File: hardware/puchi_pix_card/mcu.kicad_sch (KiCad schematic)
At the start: 47 parts, among them J1 USB_C_Receptacle_USB2.0_14P, J2 Conn_01x04, J3 Conn_01x10, J4 Conn_01x10, SW1 VBAT_SW, SW2 SW_Push, SW3 SW_Push, U1 TPS61023DRL, U2 XC6206PxxxMR, U3 STM32G0B1CBTx, U4 XC6206PxxxMR, U5 USBLC6-2SC6, U6 KXTJ3-1057, U7 W25Q64JVSSIQ

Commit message: Fix design-review findings: I2C/PFET-gate pull-ups, red-column VDROP, D1/L1 part selection, USB-C 16P, USB power policy, MBI GCLK dead time and sleep leak paths
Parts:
- added C16: 22pF, symbol Device:C
- added R13, R14: 2.2k, symbol Device:R
- D1: value D_Schottky -> B5819W; footprint (none) -> Diode_SMD:D_SOD-123
- D2, D3: value D_Schottky -> BAT54; footprint (none) -> Diode_SMD:D_SOD-323
- J1: value USB_C_Receptacle_USB2.0_14P -> USB_C_Receptacle_USB2.0_16P; symbol Connector:USB_C_Receptacle_USB2.0_14P -> Connector:USB_C_Receptacle_USB2.0_16P
- L1: value 1uH -> SWPA4030S1R0MT; LCSC (none) -> C316359
- R10, R11: value 4.7M -> 1M
- R6, R7: value 100k -> 10k
- R8: value 10k -> 2.2k
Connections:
- net +5V: now also C16.2
- net PB6: now also R13.2
- net PB7: now also R14.2
- net at C14.1, C5.1, C6.1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: now also R13.1, R14.1
- net at R1.2, R2.2, U1.1 (FB): now also C16.1
- no-connect marks 5 -> 7

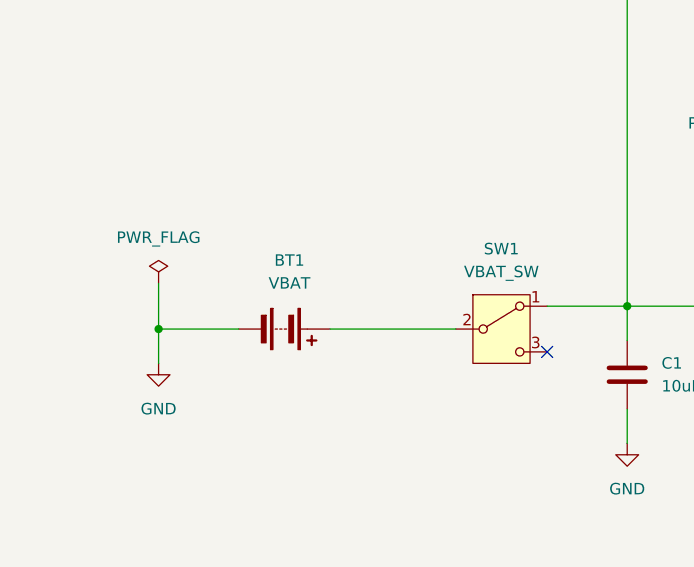
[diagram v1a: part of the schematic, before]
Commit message: Assign footprints: project footprint library (LED/MBI/inductor/switches) and bulk 0402/0805 pass
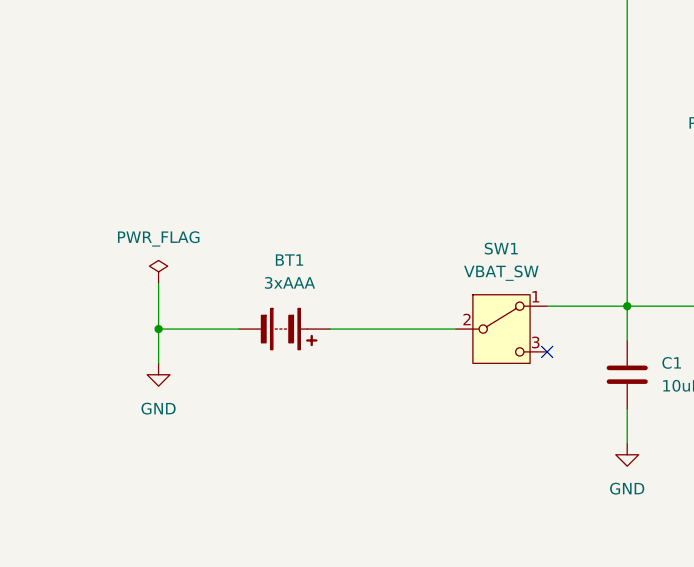
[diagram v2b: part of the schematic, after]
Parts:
- BT1: value VBAT -> 3xAAA
- C1, C2, C3: footprint (none) -> Capacitor_SMD:C_0805_2012Metric
- C10, C11, C12, C13, C14, C15, C16, C4, C5, C6, C7, C8, C9: footprint (none) -> Capacitor_SMD:C_0402_1005Metric
- D4: footprint (none) -> LED_SMD:LED_0603_1608Metric
- J1: footprint (none) -> Connector_USB:USB_C_Receptacle_HRO_TYPE-C-31-M-12
- J2: footprint (none) -> Connector_PinHeader_2.54mm:PinHeader_1x04_P2.54mm_Vertical
- J3, J4: footprint (none) -> Connector_PinHeader_2.54mm:PinHeader_1x10_P2.54mm_Vertical
- L1: footprint (none) -> puchi_pix_card:L_SWPA4030S
- R1, R10, R11, R12, R13, R14, R2, R3, R4, R5, R6, R7, R8, R9: footprint (none) -> Resistor_SMD:R_0402_1005Metric
- SW1: footprint (none) -> puchi_pix_card:SW-SMD_MST-12D18G4-SPDT-SLIDE-SWITCH
- SW2, SW3: footprint (none) -> puchi_pix_card:KEY-SMD_4P-L4.2-W3.2-P2.20-LS4.6
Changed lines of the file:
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@@
 			)
 		)
-		(property "Footprint" ""
+		(property "Footprint" "Connector_PinHeader_2.54mm:PinHeader_1x10_P2.54mm_Vertical"
 			(at 398.78 149.86 0)
 			(effects
@@
 			)
 		)
-		(property "Footprint" ""
+		(property "Footprint" "Resistor_SMD:R_0402_1005Metric"
 			(at 212.852 119.38 90)
 			(effects
@@
 			)
 		)
-		(property "Footprint" ""
+		(property "Footprint" "Capacitor_SMD:C_0402_1005Metric"
 			(at 329.8952 50.8 0)
 			(effects
@@
 			)
 		)
-		(property "Footprint" ""
+		(property "Footprint" "Capacitor_SMD:C_0402_1005Metric"
 			(at 174.9552 200.66 0)
 			(effects
@@
 			)
 		)
-		(property "Footprint" ""
+		(property "Footprint" "Resistor_SMD:R_0402_1005Metric"
 			(at 253.492 203.2 90)
 			(effects
@@
 			)
 		)
-		(property "Footprint" ""
+		(property "Footprint" "Capacitor_SMD:C_0805_2012Metric"
 			(at 83.5152 107.95 0)
 			(effects
@@
 			)
 		)
-		(property "Footprint" ""
+		(property "Footprint" "Resistor_SMD:R_0402_1005Metric"
 			(at 102.362 111.76 90)
 			(effects
@@
 			)
 		)
-		(property "Footprint" ""
+		(property "Footprint" "Capacitor_SMD:C_0402_1005Metric"
 			(at 215.5952 200.66 0)
 			(effects
@@
 			)
 		)
-		(property "Footprint" ""
+		(property "Footprint" "Resistor_SMD:R_0402_1005Metric"
 			(at 135.128 111.76 90)
 			(effects
@@
 			)
 		)
-		(property "Footprint" ""
+		(property "Footprint" "Capacitor_SMD:C_0805_2012Metric"
 			(at 164.7952 115.57 0)
 			(effects
@@
 			)
 		)
-		(property "Footprint" ""
+		(property "Footprint" "Capacitor_SMD:C_0402_1005Metric"
 			(at 199.0852 116.84 0)
 			(effects
@@
 			)
 		)
-		(property "Footprint" ""
+		(property "Footprint" "Connector_PinHeader_2.54mm:PinHeader_1x10_P2.54mm_Vertical"
 			(at 398.78 106.68 0)
 			(effects
@@
 			)
 		)
-		(property "Footprint" ""
+		(property "Footprint" "Capacitor_SMD:C_0402_1005Metric"
 			(at 277.8252 201.93 0)
 			(effects
@@
 			)
 		)
-		(property "Value" "VBAT"
+		(property "Value" "3xAAA"
 			(at 45.0215 93.98 90)
 			(effects
@@
 			)
 		)
-		(property "Footprint" ""
+		(property "Footprint" "Resistor_SMD:R_0402_1005Metric"
 			(at 257.81 112.522 90)
 			(effects
@@
 			)
 		)
-		(property "Footprint" ""
+		(property "Footprint" "Capacitor_SMD:C_0402_1005Metric"
 			(at 136.8552 52.07 0)
 			(effects
@@
 			)
 		)
-		(property "Footprint" ""
+		(property "Footprint" "puchi_pix_card:KEY-SMD_4P-L4.2-W3.2-P2.20-LS4.6"
 			(at 232.41 86.36 0)
 			(effects
@@
 			)
 		)
-		(property "Footprint" ""
+		(property "Footprint" "Capacitor_SMD:C_0402_1005Metric"
 			(at 146.05 124.7648 0)
 			(effects
@@
 			)
 		)
-		(property "Footprint" ""
+		(property "Footprint" "puchi_pix_card:KEY-SMD_4P-L4.2-W3.2-P2.20-LS4.6"
 			(at 201.93 49.53 0)
 			(effects
@@
 			)
 		)
-		(property "Footprint" ""
+		(property "Footprint" "LED_SMD:LED_0603_1608Metric"
 			(at 246.38 114.3 0)
 			(effects
@@
 			)
 		)
-		(property "Footprint" ""
+		(property "Footprint" "Capacitor_SMD:C_0402_1005Metric"
 			(at 357.8352 50.8 0)
 			(effects
@@
 			)
 		)
-		(property "Footprint" ""
+		(property "Footprint" "Capacitor_SMD:C_0402_1005Metric"
 			(at 88.5952 142.24 0)
 			(effects
@@
 			)
 		)
-		(property "Footprint" ""
+		(property "Footprint" "Capacitor_SMD:C_0402_1005Metric"
 			(at 343.8652 50.8 0)
 			(effects
@@
 			)
 		)
-		(property "Footprint" ""
+		(property "Footprint" "Capacitor_SMD:C_0402_1005Metric"
 			(at 106.3752 52.07 0)
 			(effects
@@
 			)
 		)
-		(property "Footprint" ""
+		(property "Footprint" "Resistor_SMD:R_0402_1005Metric"
 			(at 69.85 172.212 90)
 			(effects
@@
 			)
 		)
-		(property "Footprint" ""
+		(property "Footprint" "Resistor_SMD:R_0402_1005Metric"
 			(at 77.47 183.642 90)
 			(effects
@@
 			)
 		)
-		(property "Footprint" ""
+		(property "Footprint" "Capacitor_SMD:C_0402_1005Metric"
 			(at 58.1152 162.56 0)
 			(effects
@@
 			)
 		)
-		(property "Footprint" ""
+		(property "Footprint" "Connector_USB:USB_C_Receptacle_HRO_TYPE-C-31-M-12"
 			(at 35.56 193.04 0)
 			(effects
@@
 			)
 		)
-		(property "Footprint" ""
+		(property "Footprint" "Connector_PinHeader_2.54mm:PinHeader_1x04_P2.54mm_Vertical"
 			(at 267.97 59.69 0)
 			(effects
@@
 			)
 		)
-		(property "Footprint" ""
+		(property "Footprint" "Resistor_SMD:R_0402_1005Metric"
 			(at 221.742 119.38 90)
 			(effects
@@
 			)
 		)
-		(property "Footprint" ""
+		(property "Footprint" "Resistor_SMD:R_0402_1005Metric"
 			(at 22.352 264.16 90)
 			(effects
@@
 			)
 		)
-		(property "Footprint" ""
+		(property "Footprint" "puchi_pix_card:L_SWPA4030S"
 			(at 101.6 85.09 0)
 			(effects
@@
 			)
 		)
-		(property "Footprint" ""
+		(property "Footprint" "Capacitor_SMD:C_0402_1005Metric"
 			(at 252.4252 88.9 0)
 			(effects
@@
 			)
 		)
-		(property "Footprint" ""
+		(property "Footprint" "Resistor_SMD:R_0402_1005Metric"
 			(at 218.44 55.372 90)
 			(effects
@@
 			)
 		)
-		(property "Footprint" ""
+		(property "Footprint" "puchi_pix_card:SW-SMD_MST-12D18G4-SPDT-SLIDE-SWITCH"
 			(at 68.58 99.06 0)
 			(effects
@@
 			)
 		)
-		(property "Footprint" ""
+		(property "Footprint" "Resistor_SMD:R_0402_1005Metric"
 			(at 22.352 250.19 90)
 			(effects
@@
 			)
 		)
-		(property "Footprint" ""
+		(property "Footprint" "Resistor_SMD:R_0402_1005Metric"
 			(at 92.202 120.65 90)
 			(effects
@@
 			)
 		)
-		(property "Footprint" ""
+		(property "Footprint" "Capacitor_SMD:C_0805_2012Metric"
 			(at 153.3652 115.57 0)
 			(effects
@@
 			)
 		)
-		(property "Footprint" ""
+		(property "Footprint" "Resistor_SMD:R_0402_1005Metric"
 			(at 92.202 134.62 90)
 			(effects
@@
 			)
 		)
-		(property "Footprint" ""
+		(property "Footprint" "Resistor_SMD:R_0402_1005Metric"
 			(at 142.24 104.902 90)
 			(effects

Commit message: Add PCB layout: 54x54 outline, 16x16 LED grid and back-side placement
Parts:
- J2: footprint Connector_PinHeader_2.54mm:PinHeader_1x04_P2.54mm_Vertical -> Connector_PinHeader_2.54mm:PinHeader_1x04_P2.54mm_Vertical_SMD_Pin1Left
- J3, J4: footprint Connector_PinHeader_2.54mm:PinHeader_1x10_P2.54mm_Vertical -> Connector_PinHeader_2.54mm:PinHeader_1x10_P2.54mm_Vertical_SMD_Pin1Left
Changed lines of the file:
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@@
 			)
 		)
-		(property "Footprint" "Connector_PinHeader_2.54mm:PinHeader_1x10_P2.54mm_Vertical"
+		(property "Footprint" "Connector_PinHeader_2.54mm:PinHeader_1x10_P2.54mm_Vertical_SMD_Pin1Left"
 			(at 398.78 149.86 0)
 			(effects
@@
 			)
 		)
-		(property "Footprint" "Connector_PinHeader_2.54mm:PinHeader_1x10_P2.54mm_Vertical"
+		(property "Footprint" "Connector_PinHeader_2.54mm:PinHeader_1x10_P2.54mm_Vertical_SMD_Pin1Left"
 			(at 398.78 106.68 0)
 			(effects
@@
 			)
 		)
-		(property "Footprint" "Connector_PinHeader_2.54mm:PinHeader_1x04_P2.54mm_Vertical"
+		(property "Footprint" "Connector_PinHeader_2.54mm:PinHeader_1x04_P2.54mm_Vertical_SMD_Pin1Left"
 			(at 267.97 59.69 0)
 			(effects

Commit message: Route the LED matrix lattice (F.Cu columns, In2 rows), place and route the back side, swap J1 to an SMD-shell USB-C, drop J3/J4
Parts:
- removed J3, J4: Conn_01x10, Connector_PinHeader_2.54mm:PinHeader_1x10_P2.54mm_Vertical_SMD_Pin1Left, symbol Connector_Generic:Conn_01x10
- J1: footprint Connector_USB:USB_C_Receptacle_HRO_TYPE-C-31-M-12 -> puchi_pix_card:USB_C_Receptacle_SHOUHAN_TYPE-C-16P-QTWT
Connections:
- net PC13: no longer names the net of U3.1 (PC13)
- net PC14: no longer names the net of U3.2 (PC14)
- net PC15: no longer names the net of U3.3 (PC15)
- no-connect marks 7 -> 22

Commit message: Swap J2 to JST SH with v1 power pin order (1:GND 2:+3V3S); replace the battery symbol with four pogo-pin contacts (VBAT/GND)
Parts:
- removed BT1: 3xAAA, symbol Device:Battery
- added BT1, BT2: POGO BT+, puchi_pix_card:Pogo_YTC1P_D2.0, symbol Connector_Generic:Conn_01x01
- added BT3, BT4: POGO BT-, puchi_pix_card:Pogo_YTC1P_D2.0, symbol Connector_Generic:Conn_01x01
- J2: value Conn_01x04 -> SWD (JST SH 4P); footprint Connector_PinHeader_2.54mm:PinHeader_1x04_P2.54mm_Vertical_SMD_Pin1Left -> Connector_JST:JST_SH_SM04B-SRSS-TB_1x04-1MP_P1.00mm_Horizontal; LCSC (none) -> C7527619
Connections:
- net BOOT/SWCLK: now also J2.4 (Pin_4); no longer J2.3 (Pin_3)
- net GND: now also J2.1 (Pin_1), BT3.1 (Pin_1), BT4.1 (Pin_1); no longer J2.4 (Pin_4)
- net SWDIO: now also J2.3 (Pin_3); no longer J2.2 (Pin_2)
- net +3V3S: now reaches C14.1, C5.1, C6.1, C7.1, C8.1, R13.1, R14.1, SW3.2, U2.2 (VO), U3.4 (VBAT), U3.5 (VREF+), U3.6 (VDD), U6.10 (VDD), U6.11 (IO_VDD), U6.3 (IO_VDD), U6.7 (VDD)
- net +3V3S: now also J2.2 (Pin_2); no longer J2.1 (Pin_1)
- net VBAT: now reaches SW1.2 (B)
- net VBAT: now also BT1.1 (Pin_1), BT2.1 (Pin_1)

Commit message: Fill LCSC part numbers for JLCPCB assembly; switch the column drivers to MBI5124GP-B (pin 21 GCLK -> /OE, net MBI_OE); R2 133k, in-stock LED/NOR listings
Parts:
- C1: LCSC (none) -> C380332
- C10, C11, C4, C5, C9: LCSC (none) -> C52923
- C12, C13, C14, C15, C6, C7: LCSC (none) -> C309458
- C16: LCSC (none) -> C1555
- C2, C3: LCSC (none) -> C45783
- C8: LCSC (none) -> C23733
- D1: LCSC (none) -> C8598
- D2, D3: LCSC (none) -> C22629
- D4: LCSC (none) -> C12624
- J1: value USB_C_Receptacle_USB2.0_16P -> TYPE-C 16P QTWT; LCSC (none) -> C5187472
- R1, R10, R11, R3: LCSC (none) -> C26083
- R12, R6, R7: LCSC (none) -> C25744
- R13, R14, R8: LCSC (none) -> C25879
- R2: value 135k -> 133k; LCSC (none) -> C25753
- R4, R5: LCSC (none) -> C25905
- R9: LCSC (none) -> C11702
- SW1: LCSC (none) -> C49023767
- SW2, SW3: LCSC (none) -> C139797
- U1: LCSC (none) -> C919459
- U2, U4: value XC6206PxxxMR -> XC6206P332MR; LCSC (none) -> C5446
- U3: LCSC (none) -> C2847904
- U5: LCSC (none) -> C7519
- U6: LCSC (none) -> C442603
- U7: LCSC (none) -> C179171
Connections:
- net GCLK renamed MBI_OE

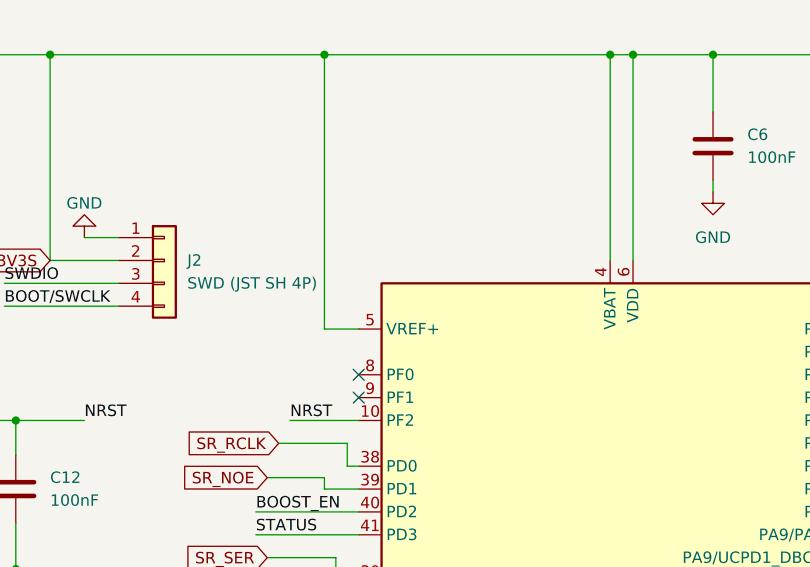
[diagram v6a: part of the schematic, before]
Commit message: Review fixes: guard the first plane against ISR re-entry, SPI2 8 MHz for the 3.3V chain delay, release the KXTJ3 latched INT, force /OE high on stop; J2 real part name and footprint id; drop MBI5153 leftovers
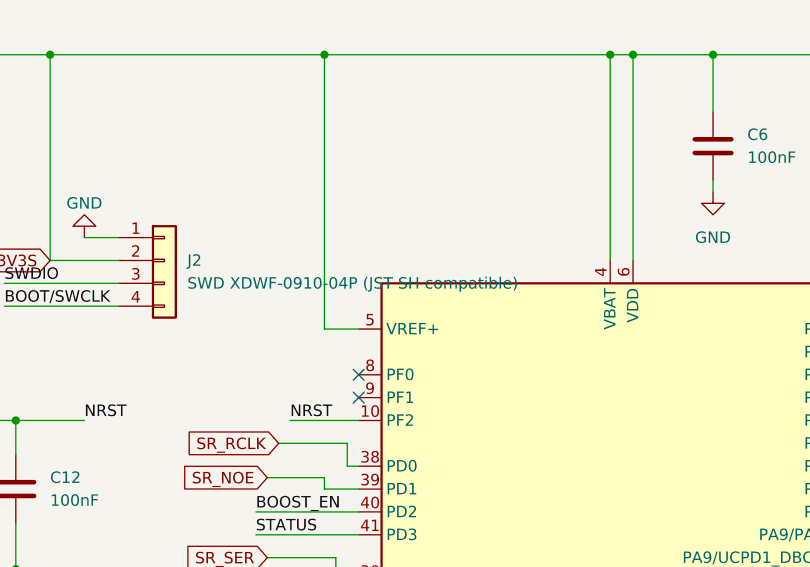
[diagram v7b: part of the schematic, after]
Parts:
- J2: value SWD (JST SH 4P) -> SWD XDWF-0910-04P (JST SH compatible)
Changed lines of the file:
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@@
 			)
 		)
-		(property "Value" "SWD (JST SH 4P)"
+		(property "Value" "SWD XDWF-0910-04P (JST SH compatible)"
 			(at 270.51 62.2299 0)
 			(effects

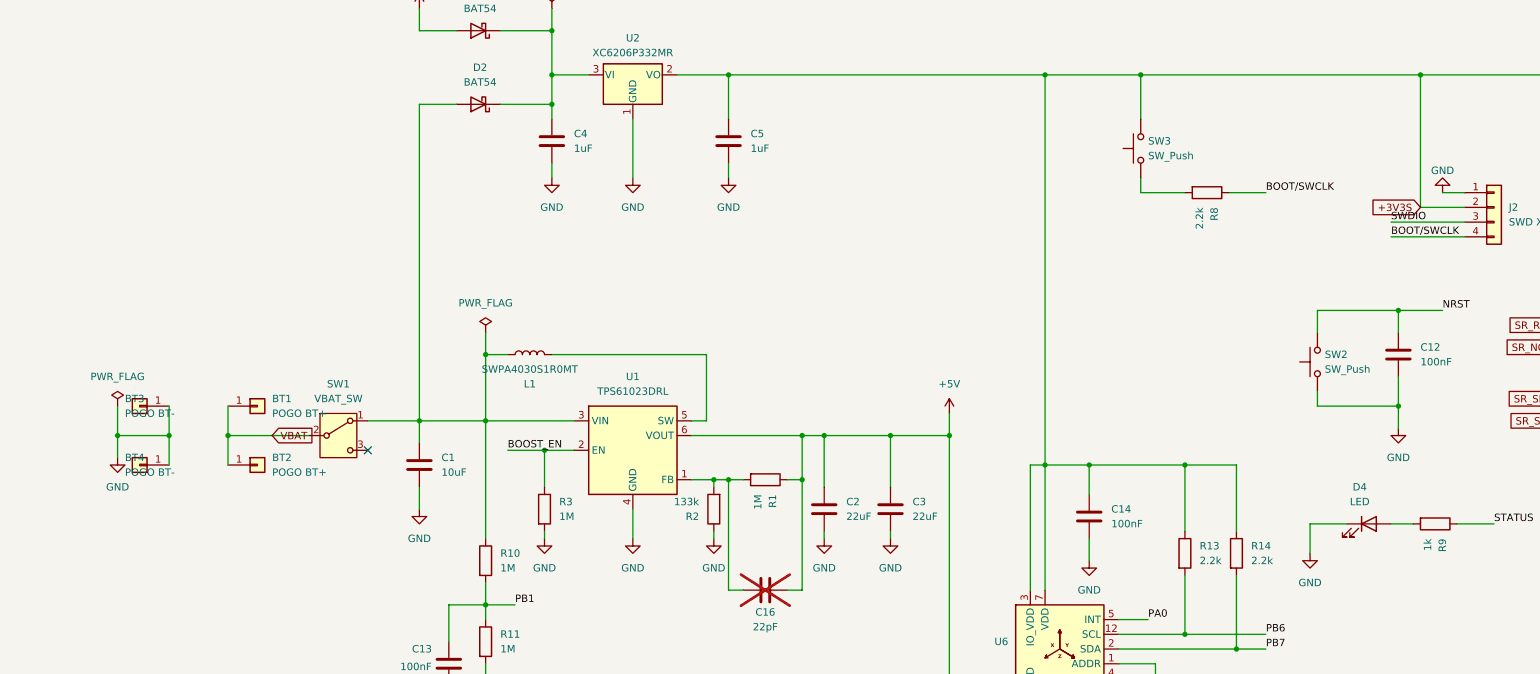
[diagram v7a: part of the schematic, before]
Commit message: Move SW1 into the +3V3S branch (boost VIN on VBAT) so the 0.1A switch carries only the MCU rail; R101 2.0k / red series 120R for the MBI5124 10mA limit and USB headroom; R9 4.7k; C1 next to U1; In1 GND plane rejoined
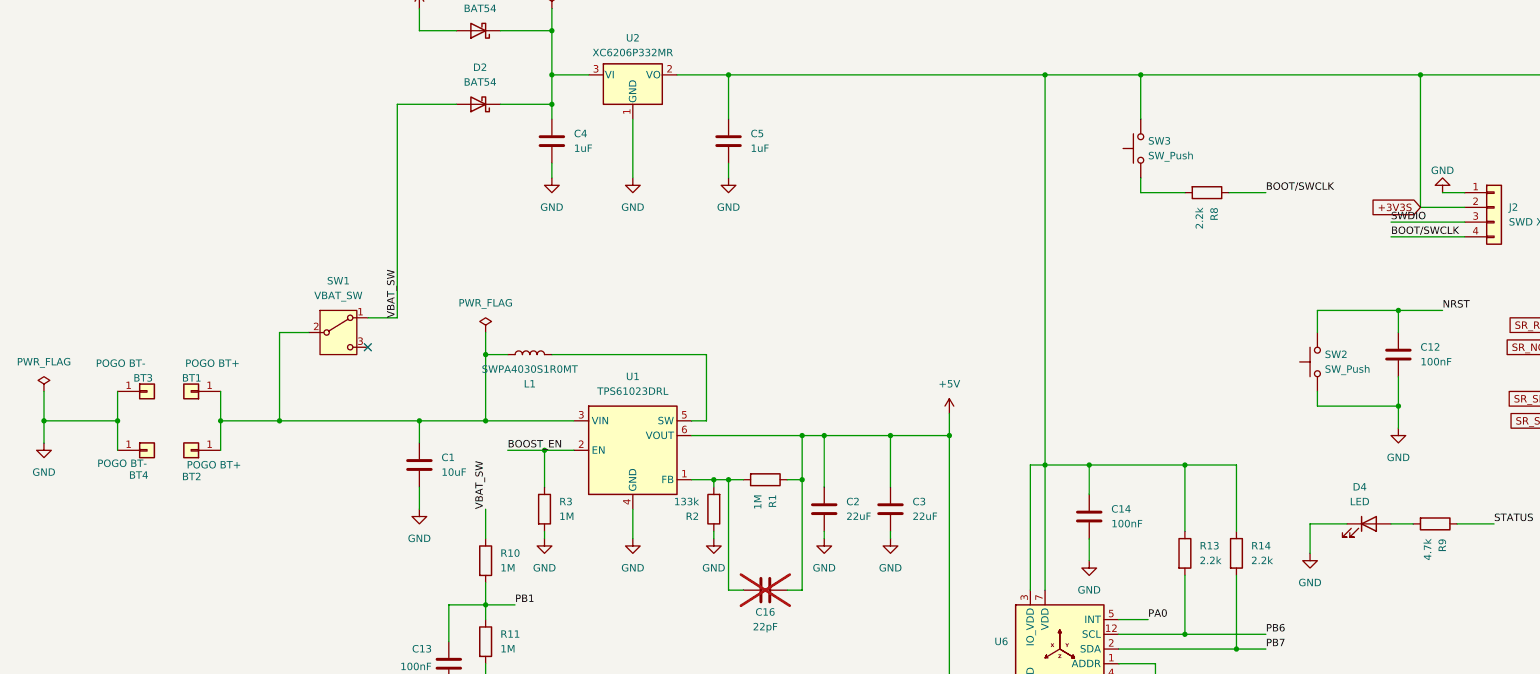
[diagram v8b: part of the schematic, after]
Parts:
- R9: value 1k -> 4.7k; LCSC C11702 -> C25900
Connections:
- net VBAT is gone; now on an unnamed net: BT1.1 (Pin_1), BT2.1 (Pin_1), SW1.2 (B)
- net at C1.1, L1.1, U1.3 (VIN): no longer D2.2 (A), R10.1, SW1.1 (A)
- new net VBAT_SW: D2.2 (A), R10.1, SW1.1 (A)
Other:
- moved on the sheet: BT1, BT2, BT3, BT4, SW1
